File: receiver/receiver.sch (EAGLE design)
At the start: 3 parts, among them Q1 3.3

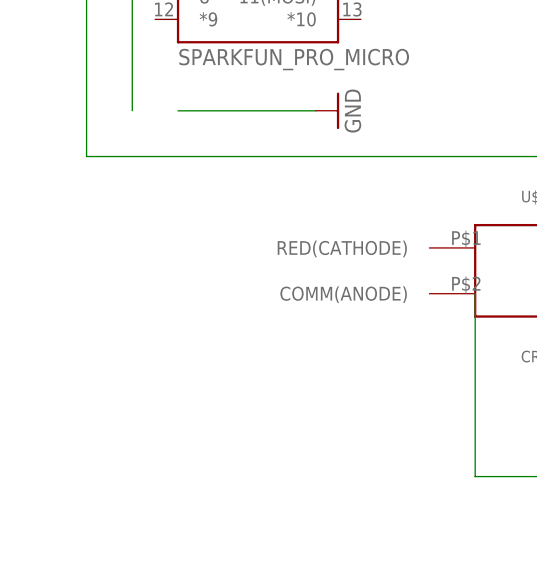
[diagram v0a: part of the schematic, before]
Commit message: add yc164 resistor to receiver
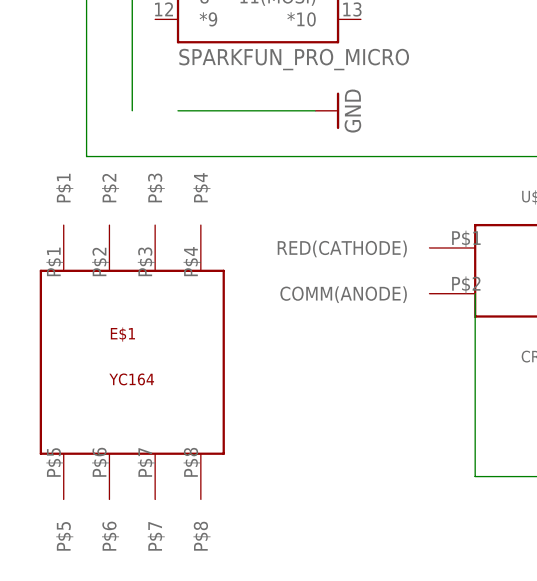
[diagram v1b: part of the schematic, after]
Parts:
- added E$1: YC164, yc164:YC164
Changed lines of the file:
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@@
 <part name="GND5" library="supply1" library_urn="urn:adsk.eagle:library:371" deviceset="GND" device=""/>
 <part name="U$1" library="cree_plcc4_rgb_led" deviceset="CREE_PLCC4_RGB_LED" device=""/>
+<part name="E$1" library="yc164" deviceset="YC164" device=""/>
 </parts>
 <sheets>
@@
 <instance part="GND5" gate="1" x="88.9" y="96.52"/>
 <instance part="U$1" gate="G$1" x="76.2" y="66.04"/>
+<instance part="E$1" gate="G$1" x="30.48" y="55.88"/>
 </instances>
 <busses>

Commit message: layout components
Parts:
- added U$2: CORE51822B, core51822b:CORE51822B
- added U$3: YC164, yc164:YC164
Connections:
- new net N$10: U$1.GREEN(CATHODE), U$3.P$6
- new net N$11: U$1.RED(CATHODE), U$3.P$5
- new net N$12: U$3.P$2, U$3.P$3
- new net N$14: U$1.BLUE(CATHODE), U$3.P$8
- new net N$7: B1.TXO, E$1.P$7, E$1.P$8
- new net N$8: E$1.P$1, E$1.P$2, E$1.P$3, E$1.P$4, U$2.P25
- net GND: now also E$1.P$5, U$2.GND0, U$2.GND1
- net N$3: now also U$3.P$4
- net N$4: now also U$3.P$1
- net N$5: now also U$3.P$7
- net VCC: now also U$2.VCC
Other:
- moved on the sheet: E$1, U$1
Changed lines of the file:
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@@
 <part name="U$1" library="cree_plcc4_rgb_led" deviceset="CREE_PLCC4_RGB_LED" device=""/>
 <part name="E$1" library="yc164" deviceset="YC164" device=""/>
+<part name="U$2" library="core51822b" deviceset="CORE51822B" device=""/>
+<part name="P+2" library="supply1" library_urn="urn:adsk.eagle:library:371" deviceset="VCC" device=""/>
+<part name="GND7" library="supply1" library_urn="urn:adsk.eagle:library:371" deviceset="GND" device=""/>
+<part name="GND8" library="supply1" library_urn="urn:adsk.eagle:library:371" deviceset="GND" device=""/>
+<part name="U$3" library="yc164" deviceset="YC164" device=""/>
+<part name="GND6" library="supply1" library_urn="urn:adsk.eagle:library:371" deviceset="GND" device=""/>
 </parts>
 <sheets>
@@
 <instance part="P+1" gate="VCC" x="106.68" y="121.92" rot="R270"/>
 <instance part="GND5" gate="1" x="88.9" y="96.52"/>
-<instance part="U$1" gate="G$1" x="76.2" y="66.04"/>
-<instance part="E$1" gate="G$1" x="30.48" y="55.88"/>
+<instance part="U$1" gate="G$1" x="119.38" y="33.02"/>
+<instance part="E$1" gate="G$1" x="71.12" y="-2.54"/>
+<instance part="U$2" gate="G$1" x="30.48" y="45.72"/>
+<instance part="P+2" gate="VCC" x="2.54" y="25.4" rot="R180"/>
+<instance part="GND7" gate="1" x="-7.62" y="60.96" rot="R270"/>
+<instance part="GND8" gate="1" x="-5.08" y="35.56" rot="R270"/>
+<instance part="U$3" gate="G$1" x="106.68" y="63.5"/>
+<instance part="GND6" gate="1" x="53.34" y="-25.4"/>
 </instances>
 <busses>
@@
 <wire x1="88.9" y1="99.06" x2="88.9" y2="101.6" width="0.1524" layer="91"/>
 </segment>
+<segment>
+<pinref part="U$2" gate="G$1" pin="GND1"/>
+<pinref part="GND8" gate="1" pin="GND"/>
+<wire x1="10.16" y1="35.56" x2="-2.54" y2="35.56" width="0.1524" layer="91"/>
+</segment>
+<segment>
+<pinref part="GND7" gate="1" pin="GND"/>
+<pinref part="U$2" gate="G$1" pin="GND0"/>
+<wire x1="-5.08" y1="60.96" x2="10.16" y2="60.96" width="0.1524" layer="91"/>
+</segment>
+<segment>
+<pinref part="E$1" gate="G$1" pin="P$5"/>
+<wire x1="63.5" y1="-12.7" x2="63.5" y2="-20.32" width="0.1524" layer="91"/>
+<wire x1="63.5" y1="-20.32" x2="53.34" y2="-20.32" width="0.1524" layer="91"/>
+<pinref part="GND6" gate="1" pin="GND"/>
+<wire x1="53.34" y1="-20.32" x2="53.34" y2="-22.86" width="0.1524" layer="91"/>
+</segment>
 </net>
 <net name="VCC" class="0">
@@
 <pinref part="P+1" gate="VCC" pin="VCC"/>
 <wire x1="101.6" y1="121.92" x2="104.14" y2="121.92" width="0.1524" layer="91"/>
+</segment>
+<segment>
+<pinref part="U$2" gate="G$1" pin="VCC"/>
+<pinref part="P+2" gate="VCC" pin="VCC"/>
+<wire x1="10.16" y1="33.02" x2="2.54" y2="33.02" width="0.1524" layer="91"/>
+<wire x1="2.54" y1="33.02" x2="2.54" y2="27.94" width="0.1524" layer="91"/>
 </segment>
 </net>
@@
 <wire x1="83.82" y1="119.38" x2="91.44" y2="119.38" width="0.1524" layer="91"/>
 <wire x1="91.44" y1="119.38" x2="91.44" y2="106.68" width="0.1524" layer="91"/>
-<wire x1="91.44" y1="106.68" x2="116.84" y2="106.68" width="0.1524" layer="91"/>
-<wire x1="116.84" y1="106.68" x2="116.84" y2="43.18" width="0.1524" layer="91"/>
+<wire x1="91.44" y1="106.68" x2="142.24" y2="106.68" width="0.1524" layer="91"/>
+<wire x1="142.24" y1="106.68" x2="142.24" y2="20.32" width="0.1524" layer="91"/>
+<wire x1="142.24" y1="20.32" x2="106.68" y2="20.32" width="0.1524" layer="91"/>
 <pinref part="U$1" gate="G$1" pin="COMM(ANODE)"/>
-<wire x1="116.84" y1="43.18" x2="68.58" y2="43.18" width="0.1524" layer="91"/>
-<wire x1="68.58" y1="43.18" x2="68.58" y2="63.5" width="0.1524" layer="91"/>
+<wire x1="111.76" y1="30.48" x2="106.68" y2="30.48" width="0.1524" layer="91"/>
+<wire x1="106.68" y1="30.48" x2="106.68" y2="20.32" width="0.1524" layer="91"/>
 </segment>
 </net>
@@
 <pinref part="B1" gate="G$1" pin="A3"/>
 <wire x1="55.88" y1="111.76" x2="78.74" y2="111.76" width="0.1524" layer="91"/>
-<wire x1="78.74" y1="111.76" x2="78.74" y2="81.28" width="0.1524" layer="91"/>
+<wire x1="78.74" y1="111.76" x2="78.74" y2="88.9" width="0.1524" layer="91"/>
+<pinref part="U$3" gate="G$1" pin="P$4"/>
+<wire x1="114.3" y1="73.66" x2="114.3" y2="88.9" width="0.1524" layer="91"/>
+<wire x1="78.74" y1="88.9" x2="114.3" y2="88.9" width="0.1524" layer="91"/>
 </segment>
 </net>
@@
 <wire x1="55.88" y1="109.22" x2="76.2" y2="109.22" width="0.1524" layer="91"/>
 <wire x1="76.2" y1="109.22" x2="76.2" y2="81.28" width="0.1524" layer="91"/>
+<wire x1="76.2" y1="81.28" x2="99.06" y2="81.28" width="0.1524" layer="91"/>
+<pinref part="U$3" gate="G$1" pin="P$1"/>
+<wire x1="99.06" y1="81.28" x2="99.06" y2="73.66" width="0.1524" layer="91"/>
 </segment>
 </net>
@@
 <wire x1="25.4" y1="111.76" x2="25.4" y2="78.74" width="0.1524" layer="91"/>
 <wire x1="25.4" y1="78.74" x2="76.2" y2="78.74" width="0.1524" layer="91"/>
+<wire x1="76.2" y1="78.74" x2="76.2" y2="63.5" width="0.1524" layer="91"/>
+<wire x1="76.2" y1="63.5" x2="127" y2="63.5" width="0.1524" layer="91"/>
+<pinref part="U$3" gate="G$1" pin="P$7"/>
+<wire x1="109.22" y1="53.34" x2="109.22" y2="45.72" width="0.1524" layer="91"/>
+<wire x1="109.22" y1="45.72" x2="127" y2="45.72" width="0.1524" layer="91"/>
+<wire x1="127" y1="63.5" x2="127" y2="45.72" width="0.1524" layer="91"/>
 </segment>
 </net>
@@
 </segment>
 </net>
+<net name="N$7" class="0">
+<segment>
+<pinref part="B1" gate="G$1" pin="TXO"/>
+<wire x1="33.02" y1="121.92" x2="-12.7" y2="121.92" width="0.1524" layer="91"/>
+<wire x1="-12.7" y1="121.92" x2="-12.7" y2="-35.56" width="0.1524" layer="91"/>
+<wire x1="-12.7" y1="-35.56" x2="73.66" y2="-35.56" width="0.1524" layer="91"/>
+<pinref part="E$1" gate="G$1" pin="P$8"/>
+<wire x1="73.66" y1="-35.56" x2="78.74" y2="-35.56" width="0.1524" layer="91"/>
+<wire x1="78.74" y1="-35.56" x2="78.74" y2="-12.7" width="0.1524" layer="91"/>
+<pinref part="E$1" gate="G$1" pin="P$7"/>
+<wire x1="73.66" y1="-35.56" x2="73.66" y2="-12.7" width="0.1524" layer="91"/>
+<junction x="73.66" y="-35.56"/>
+</segment>
+</net>
+<net name="N$8" class="0">
+<segment>
+<pinref part="U$2" gate="G$1" pin="P25"/>
+<wire x1="10.16" y1="48.26" x2="-7.62" y2="48.26" width="0.1524" layer="91"/>
+<wire x1="-7.62" y1="48.26" x2="-7.62" y2="10.16" width="0.1524" layer="91"/>
+<wire x1="-7.62" y1="10.16" x2="58.42" y2="10.16" width="0.1524" layer="91"/>
+<wire x1="58.42" y1="10.16" x2="58.42" y2="12.7" width="0.1524" layer="91"/>
+<wire x1="58.42" y1="12.7" x2="63.5" y2="12.7" width="0.1524" layer="91"/>
+<pinref part="E$1" gate="G$1" pin="P$4"/>
+<wire x1="63.5" y1="12.7" x2="68.58" y2="12.7" width="0.1524" layer="91"/>
+<wire x1="68.58" y1="12.7" x2="73.66" y2="12.7" width="0.1524" layer="91"/>
+<wire x1="73.66" y1="12.7" x2="78.74" y2="12.7" width="0.1524" layer="91"/>
+<wire x1="78.74" y1="12.7" x2="78.74" y2="7.62" width="0.1524" layer="91"/>
+<pinref part="E$1" gate="G$1" pin="P$3"/>
+<wire x1="73.66" y1="12.7" x2="73.66" y2="7.62" width="0.1524" layer="91"/>
+<junction x="73.66" y="12.7"/>
+<pinref part="E$1" gate="G$1" pin="P$2"/>
+<wire x1="68.58" y1="12.7" x2="68.58" y2="7.62" width="0.1524" layer="91"/>
+<junction x="68.58" y="12.7"/>
+<pinref part="E$1" gate="G$1" pin="P$1"/>
+<wire x1="63.5" y1="12.7" x2="63.5" y2="7.62" width="0.1524" layer="91"/>
+<junction x="63.5" y="12.7"/>
+</segment>
+</net>
+<net name="N$11" class="0">
+<segment>
+<pinref part="U$1" gate="G$1" pin="RED(CATHODE)"/>
+<wire x1="111.76" y1="35.56" x2="99.06" y2="35.56" width="0.1524" layer="91"/>
+<pinref part="U$3" gate="G$1" pin="P$5"/>
+<wire x1="99.06" y1="35.56" x2="99.06" y2="53.34" width="0.1524" layer="91"/>
+</segment>
+</net>
+<net name="N$10" class="0">
+<segment>
+<pinref part="U$3" gate="G$1" pin="P$6"/>
+<wire x1="104.14" y1="53.34" x2="104.14" y2="40.64" width="0.1524" layer="91"/>
+<wire x1="104.14" y1="40.64" x2="132.08" y2="40.64" width="0.1524" layer="91"/>
+<pinref part="U$1" gate="G$1" pin="GREEN(CATHODE)"/>
+<wire x1="132.08" y1="40.64" x2="132.08" y2="35.56" width="0.1524" layer="91"/>
+<wire x1="132.08" y1="35.56" x2="127" y2="35.56" width="0.1524" layer="91"/>
+</segment>
+</net>
+<net name="N$12" class="0">
+<segment>
+<pinref part="U$3" gate="G$1" pin="P$2"/>
+<wire x1="104.14" y1="73.66" x2="104.14" y2="83.82" width="0.1524" layer="91"/>
+<wire x1="104.14" y1="83.82" x2="109.22" y2="83.82" width="0.1524" layer="91"/>
+<pinref part="U$3" gate="G$1" pin="P$3"/>
+<wire x1="109.22" y1="83.82" x2="109.22" y2="73.66" width="0.1524" layer="91"/>
+</segment>
+</net>
+<net name="N$14" class="0">
+<segment>
+<pinref part="U$1" gate="G$1" pin="BLUE(CATHODE)"/>
+<wire x1="127" y1="30.48" x2="137.16" y2="30.48" width="0.1524" layer="91"/>
+<pinref part="U$3" gate="G$1" pin="P$8"/>
+<wire x1="137.16" y1="30.48" x2="137.16" y2="48.26" width="0.1524" layer="91"/>
+<wire x1="114.3" y1="53.34" x2="114.3" y2="48.26" width="0.1524" layer="91"/>
+<wire x1="114.3" y1="48.26" x2="137.16" y2="48.26" width="0.1524" layer="91"/>
+</segment>
+</net>

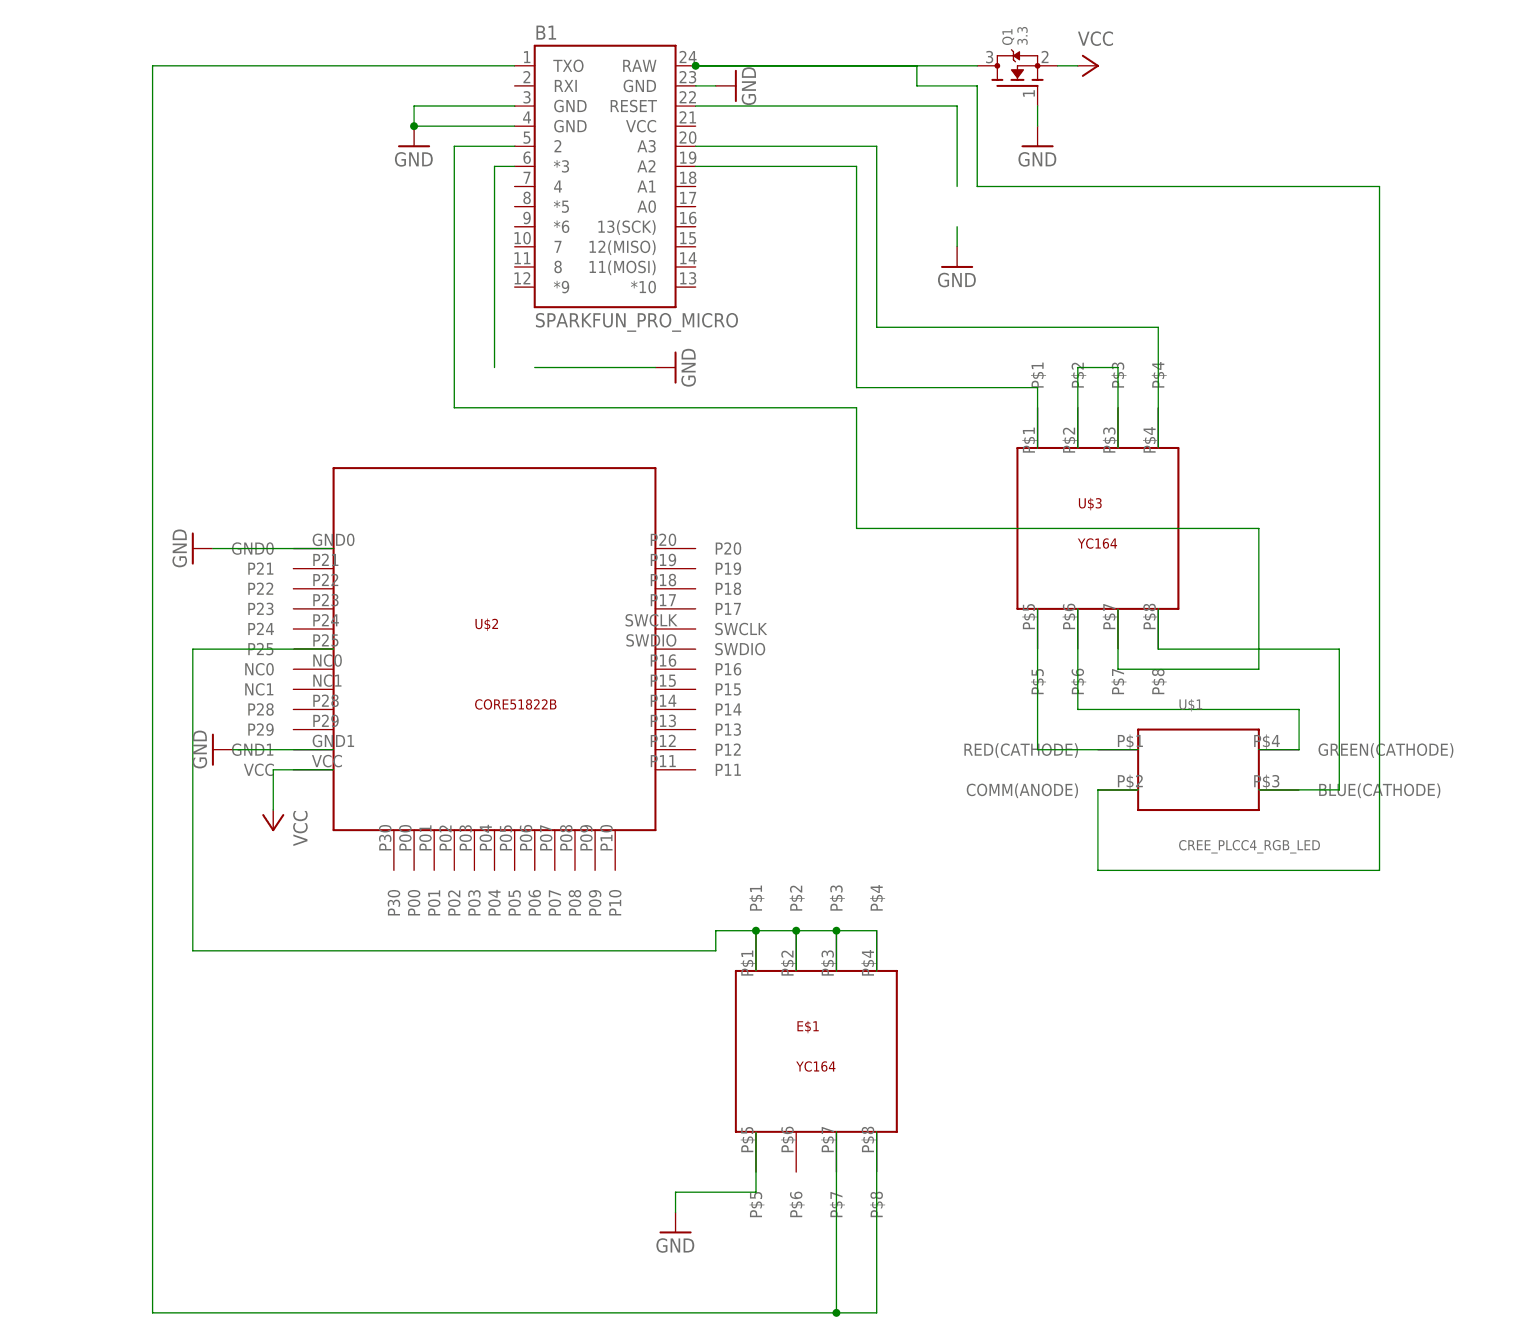
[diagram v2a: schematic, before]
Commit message: add pts525-sm15 spst push button switch
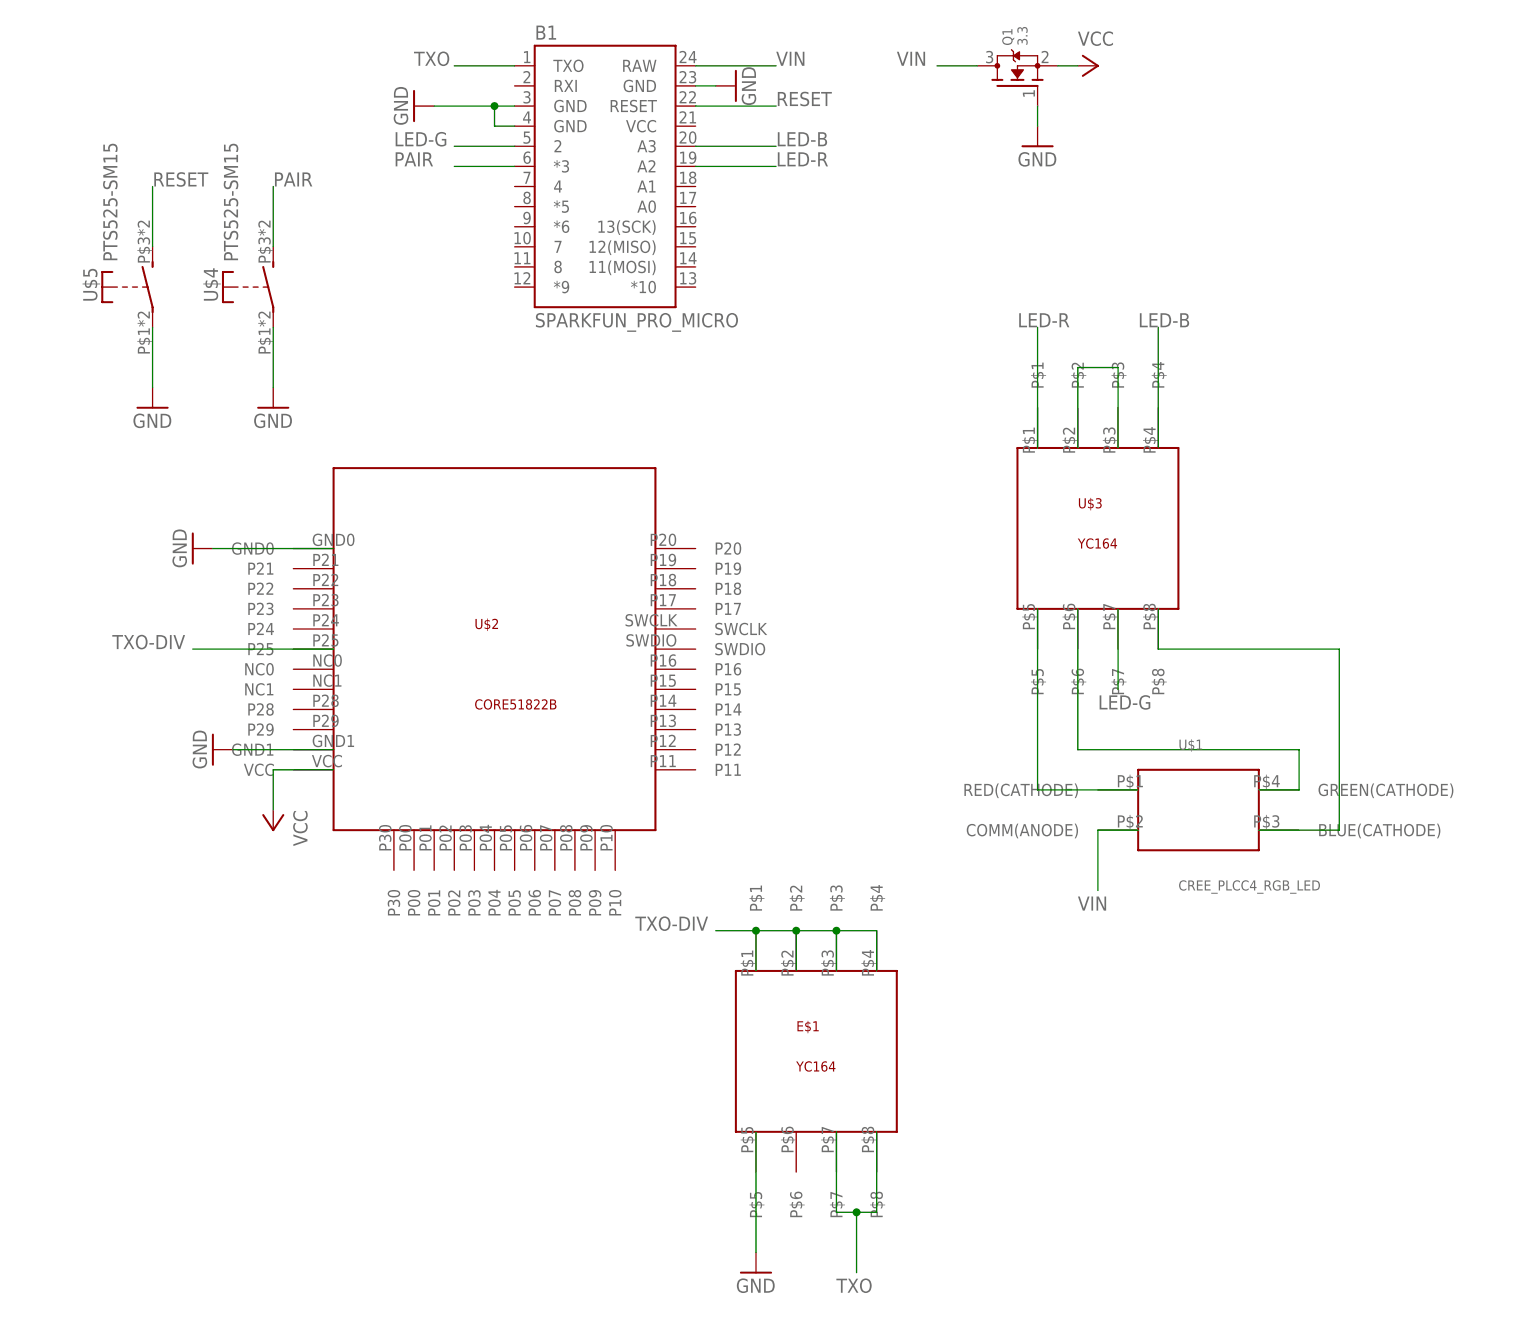
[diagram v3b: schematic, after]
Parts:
- added U$4, U$5: PTS525-SM15, pts525-sm15:PTS525-SM15
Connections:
- net N$1 renamed VIN
- net N$3 renamed LED-B
- net N$4 renamed LED-R
- net N$5 renamed LED-G
- net N$7 renamed TXO
- net N$8 renamed TXO-DIV
- removed net N$2: B1.RESET
- removed net N$6: B1.*3
- new net PAIR: B1.*3, U$4.S
- new net RESET: B1.RESET, U$5.S
- net GND: now also U$4.P, U$5.P
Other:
- moved on the sheet: U$1

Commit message: update board
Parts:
- removed B1: SPARKFUN_PRO_MICRO, SparkFun-Boards:SPARKFUN_PRO_MICRO
- added U$6, U$7: PROMICRO_HEADER, promicro_header:PROMICRO_HEADER
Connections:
- new net ???: U$2.SWCLK
- new net ????: U$2.SWDIO
- new net ????????: U$6.P$4
- new net RXI: U$2.P24, U$7.P$2
- net GND: now also U$6.P$2, U$7.P$3, U$7.P$4; no longer B1.GND, B1.GND@1, B1.GND@2
- net LED-B: now also U$6.P$5; no longer B1.A3
- net LED-G: now also U$7.P$5; no longer B1.2
- net LED-R: now also U$6.P$6; no longer B1.A2
- net PAIR: now also U$2.P29, U$7.P$6; no longer B1.*3
- net RESET: now also U$6.P$3; no longer B1.RESET
- net TXO: now also U$7.P$1; no longer B1.TXO
- net VIN: now also U$6.P$1; no longer B1.RAW
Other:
- moved on the sheet: U$4, U$5

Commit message: re-route
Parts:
- renumbered E$1 to RA2, Q1 to U2, U$1 to D1, U$2 to U1, U$3 to RA1, U$4 to B1, U$5 to B2, U$6 to P2, U$7 to P1
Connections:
- removed net ????????: P2.P$4
